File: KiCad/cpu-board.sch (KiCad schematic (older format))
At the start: 55 parts, among them CON1 BARREL_JACK, J1 Conn_FT245R, SW1 SW_PUSH_SMALL, SW2 SWITCH_INV, SW3 SW_PUSH_SMALL, U1 68008D, U10 GAL22V10, U11 74LS244, U12 LM555, U2 74LS08, U3 29F040B, U4 BS62LV4006, U5 74LS32, U6 74LS139, U7 74LS00, U8 74LS32, U9 74LS377, X1 OSCILLATOR

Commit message: add missing annotation
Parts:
- gave numbers to parts that had none: 2
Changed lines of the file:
@@
 	4400 1200 4400 1450
 $Comp
-L cpu-board-rescue:C C?
+L cpu-board-rescue:C C13
 U 1 1 5E6618CF
 P 4700 3750
-F 0 "C?" H 4700 3850 40  0000 L CNN
+F 0 "C13" H 4700 3850 40  0000 L CNN
 F 1 "0.1uF" H 4706 3665 40  0000 L CNN
 F 2 "Discret:C1" H 4738 3600 30  0001 C CNN
@@
 $EndComp
 $Comp
-L power:+5V #PWR?
+L power:+5V #PWR014
 U 1 1 5E662B43
 P 4700 3550
-F 0 "#PWR?" H 4700 3640 20  0001 C CNN
+F 0 "#PWR014" H 4700 3640 20  0001 C CNN
 F 1 "+5V" H 4700 3640 30  0000 C CNN
 F 2 "" H 4700 3550 60  0000 C CNN
@@
 $EndComp
 $Comp
-L cpu-board-rescue:GND #PWR?
+L cpu-board-rescue:GND #PWR019
 U 1 1 5E66313D
 P 4700 3950
-F 0 "#PWR?" H 4700 3950 30  0001 C CNN
+F 0 "#PWR019" H 4700 3950 30  0001 C CNN
 F 1 "GND" H 4700 3880 30  0001 C CNN
 F 2 "" H 4700 3950 60  0000 C CNN
@@
 $EndComp
 $Comp
-L cpu-board-rescue:C C?
+L cpu-board-rescue:C C14
 U 1 1 5E666AC0
 P 8500 4550
-F 0 "C?" H 8500 4650 40  0000 L CNN
+F 0 "C14" H 8500 4650 40  0000 L CNN
 F 1 "0.1uF" H 8506 4465 40  0000 L CNN
 F 2 "Discret:C1" H 8538 4400 30  0001 C CNN
@@
 $EndComp
 $Comp
-L power:+5V #PWR?
+L power:+5V #PWR021
 U 1 1 5E666AC6
 P 8500 4350
-F 0 "#PWR?" H 8500 4440 20  0001 C CNN
+F 0 "#PWR021" H 8500 4440 20  0001 C CNN
 F 1 "+5V" H 8500 4440 30  0000 C CNN
 F 2 "" H 8500 4350 60  0000 C CNN
@@
 $EndComp
 $Comp
-L cpu-board-rescue:GND #PWR?
+L cpu-board-rescue:GND #PWR025
 U 1 1 5E666ACC
 P 8500 4750
-F 0 "#PWR?" H 8500 4750 30  0001 C CNN
+F 0 "#PWR025" H 8500 4750 30  0001 C CNN
 F 1 "GND" H 8500 4680 30  0001 C CNN
 F 2 "" H 8500 4750 60  0000 C CNN

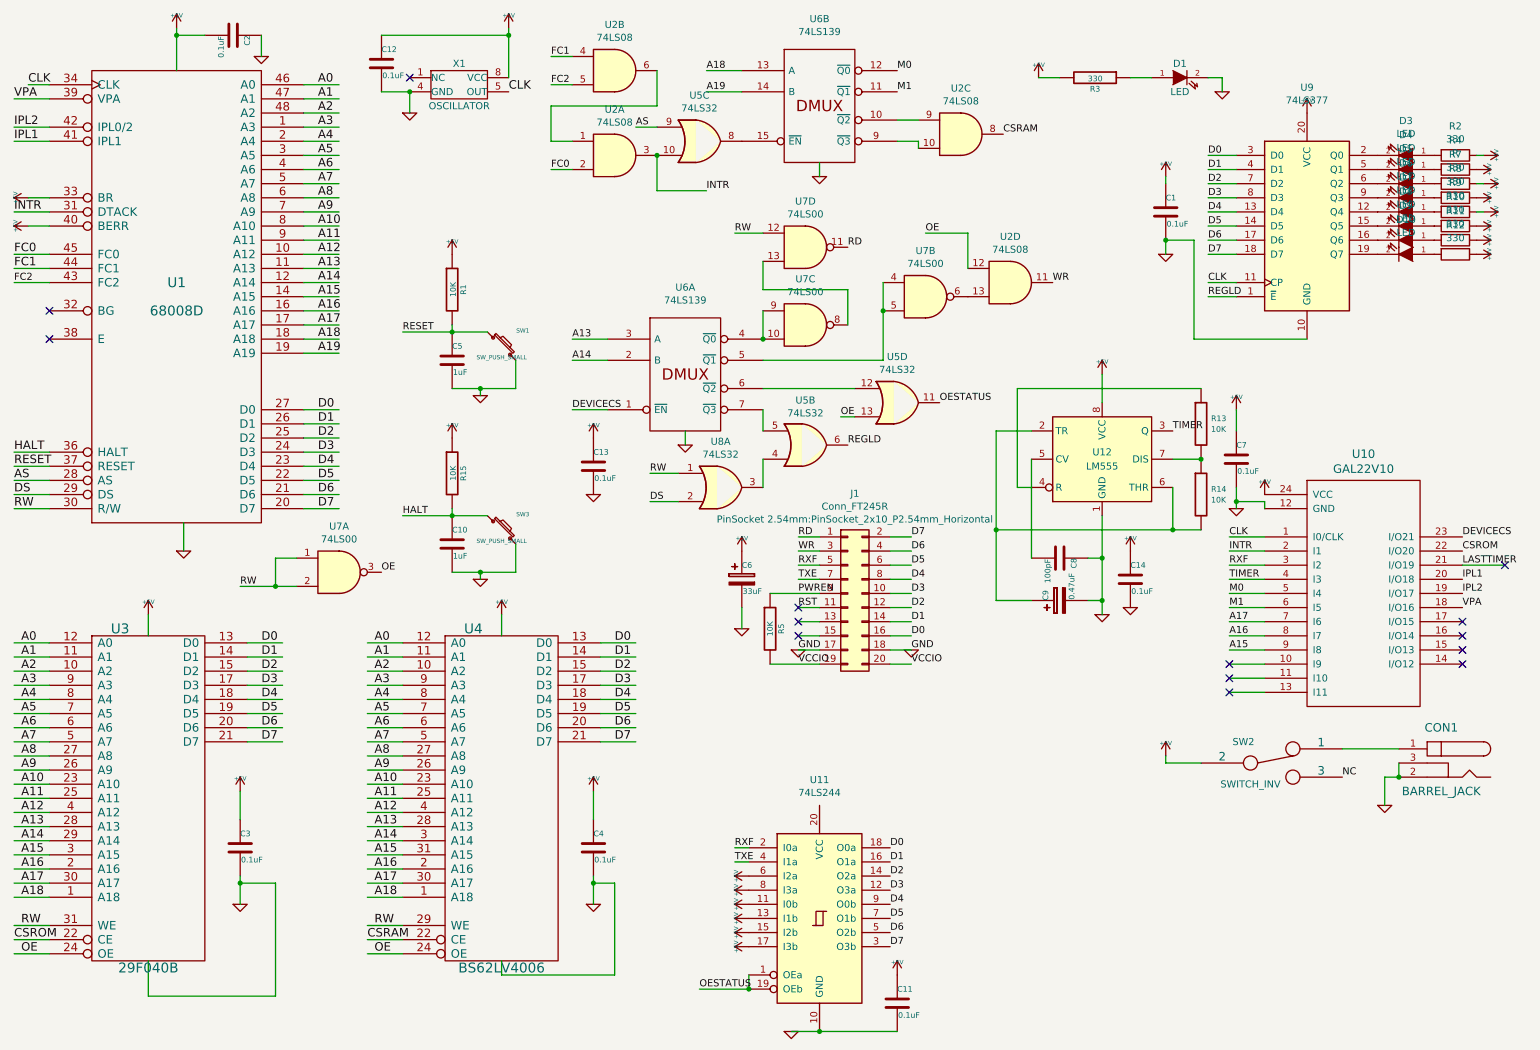
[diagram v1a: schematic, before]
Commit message: add footprints to schema, add chips to board layout
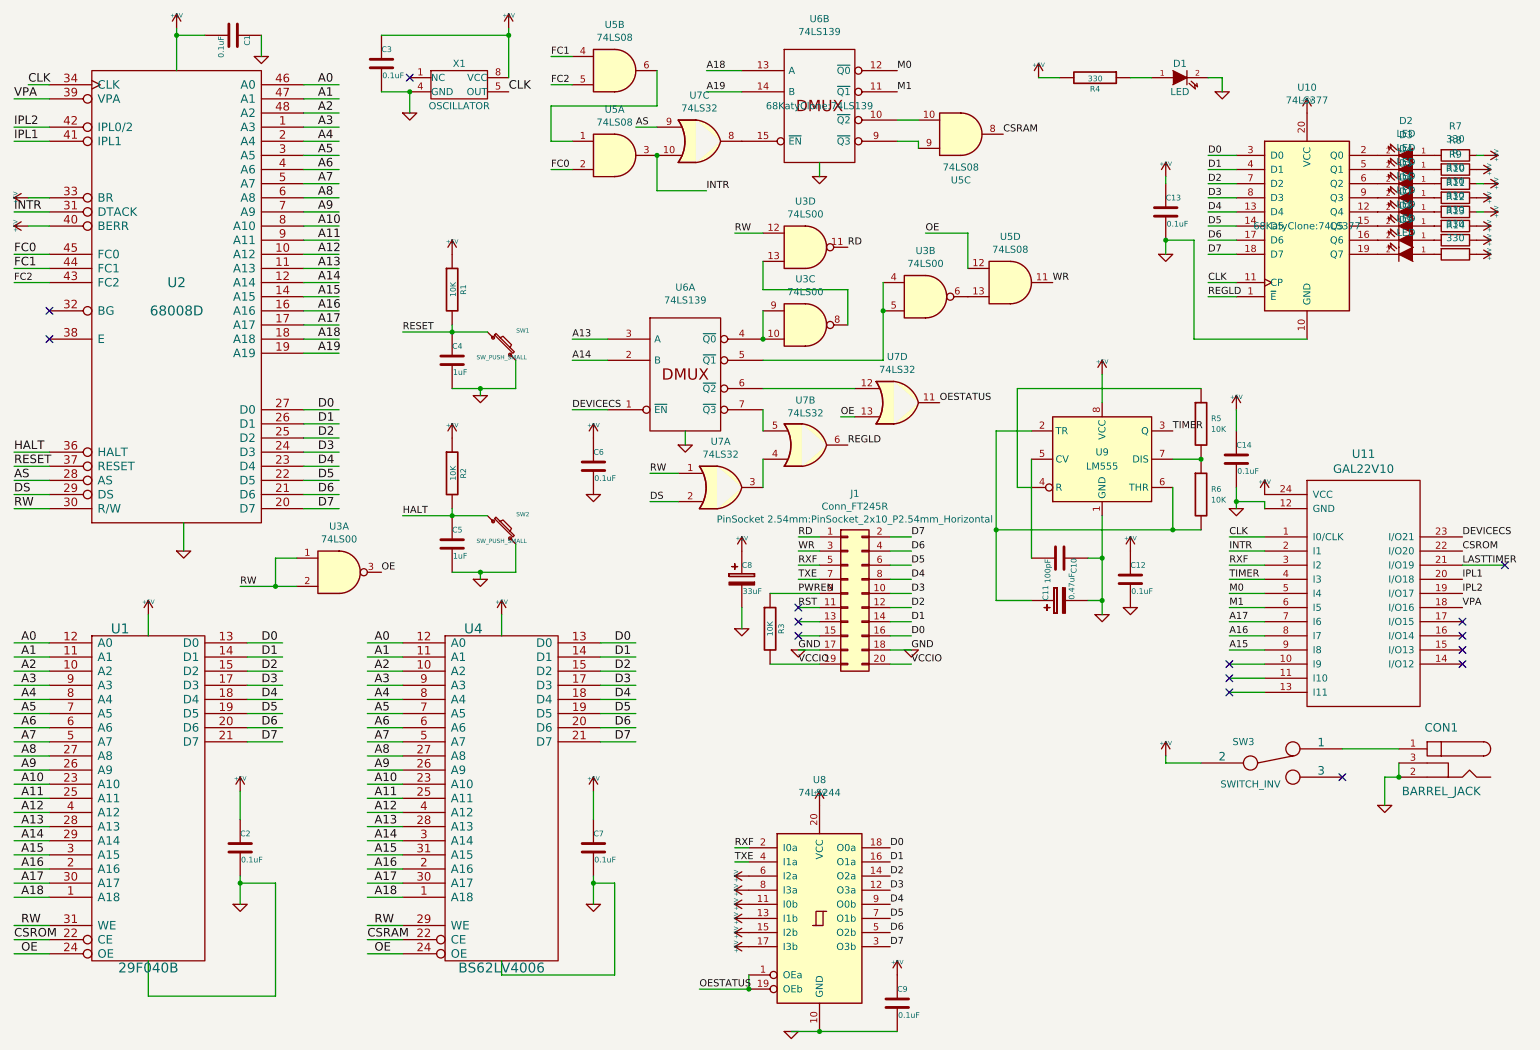
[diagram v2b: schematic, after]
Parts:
- U1: renamed from U3; footprint Sockets_DIP:DIP-32__600_ELL -> 68KatyClone:DIP-32_W15.24mm_Socket_LongPads
- U10: renamed from U9; footprint (none) -> 68KatyClone:74LS377
- U11: renamed from U10; footprint (none) -> 68KatyClone:GAL22V10
- U2: renamed from U1; footprint Sockets_DIP:DIP-48__600_ELL -> 68KatyClone:DIP-48_W15.24mm_Socket_LongPads
- U3: renamed from U7; footprint (none) -> 68KatyClone:DIP-14_W7.62mm_Socket_LongPads
- U4: footprint Sockets_DIP:DIP-32__600_ELL -> 68KatyClone:DIP-32_W15.24mm_Socket_LongPads
- U5: renamed from U2; footprint (none) -> 68KatyClone:DIP-14_W7.62mm_Socket_LongPads
- U6: footprint (none) -> 68KatyClone:74LS139
- U7: renamed from U5; footprint (none) -> 68KatyClone:DIP-14_W7.62mm_Socket_LongPads
- U7: renamed from U8; footprint (none) -> 68KatyClone:DIP-14_W7.62mm_Socket_LongPads
- U9: renamed from U12; footprint (none) -> 68KatyClone:DIP-8_W7.62mm_Socket_LongPads
- X1: footprint Sockets_DIP:DIP-8__300_ELL -> 68KatyClone:DIP-8_W7.62mm_Socket_LongPads
- renumbered C2 to C1, C8 to C10, C9 to C11, C14 to C12, C1 to C13, C7 to C14, C3 to C2, C12 to C3, C5 to C4, C10 to C5, C13 to C6, C4 to C7, C6 to C8, C11 to C9, D3 to D2, D4 to D3, D5 to D4, D6 to D5, D7 to D6, D8 to D7, D9 to D8, D10 to D9, R8 to R10, R9 to R11, R10 to R12, R11 to R13, R12 to R14, R15 to R2, R5 to R3, R3 to R4, R13 to R5, R14 to R6, R2 to R7, R4 to R8, R7 to R9, SW3 to SW2, SW2 to SW3, U11 to U8
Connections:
- net labels removed: NC
- no-connect marks 14 -> 15

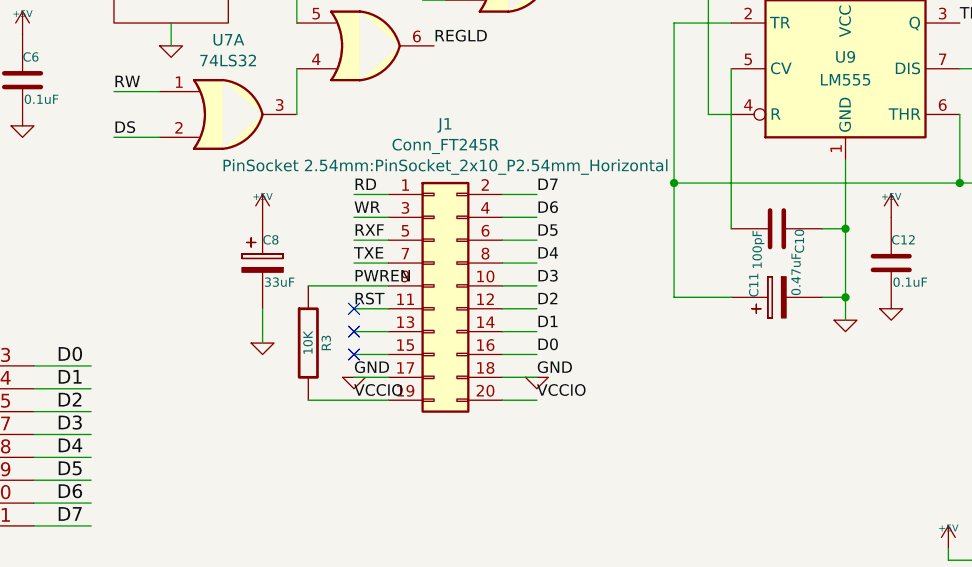
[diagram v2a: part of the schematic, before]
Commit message: add missing pull-up resistors for TXE and RXF
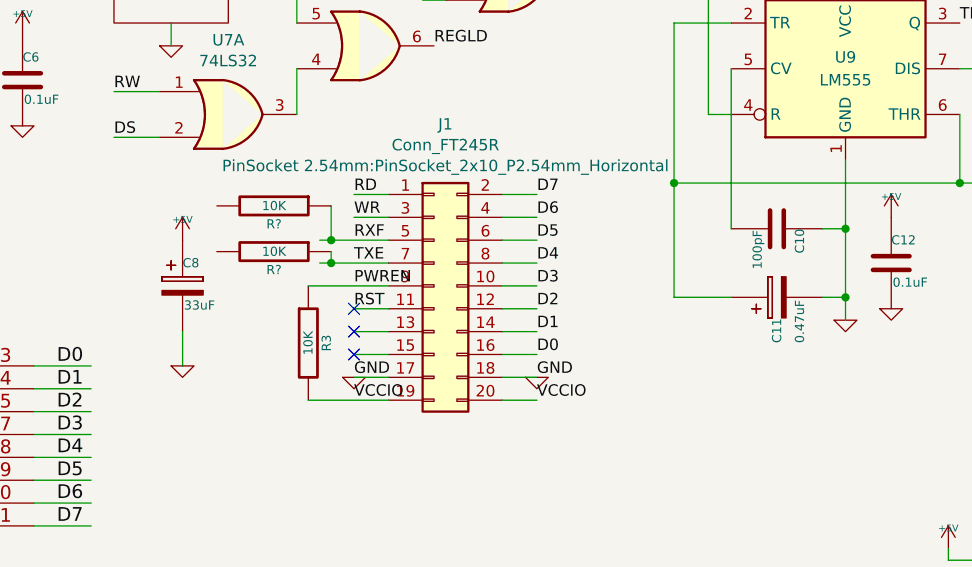
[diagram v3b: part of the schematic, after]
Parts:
- added R? (x2): 10K, Discret:R3-5, symbol cpu-board-rescue:R
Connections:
- wire segments 274 -> 278
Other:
- moved on the sheet: C8
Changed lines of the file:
@@
 L cpu-board-rescue:CP2 C8
 U 1 1 54869317
-P 5750 4550
-F 0 "C8" H 5750 4650 40  0000 L CNN
-F 1 "33uF" H 5756 4465 40  0000 L CNN
-F 2 "Discret:C1" H 5788 4400 30  0001 C CNN
-F 3 "" H 5750 4550 60  0000 C CNN
-	1    5750 4550
+P 5400 4650
+F 0 "C8" H 5400 4750 40  0000 L CNN
+F 1 "33uF" H 5406 4565 40  0000 L CNN
+F 2 "Discret:C1" H 5438 4500 30  0001 C CNN
+F 3 "" H 5400 4650 60  0000 C CNN
+	1    5400 4650
 	1    0    0    -1
 $EndComp
@@
 L power:+5V #PWR021
 U 1 1 548819AF
-P 5750 4350
-F 0 "#PWR021" H 5750 4440 20  0001 C CNN
-F 1 "+5V" H 5750 4440 30  0000 C CNN
-F 2 "" H 5750 4350 60  0000 C CNN
-F 3 "" H 5750 4350 60  0000 C CNN
-	1    5750 4350
+P 5400 4450
+F 0 "#PWR021" H 5400 4540 20  0001 C CNN
+F 1 "+5V" H 5400 4540 30  0000 C CNN
+F 2 "" H 5400 4450 60  0000 C CNN
+F 3 "" H 5400 4450 60  0000 C CNN
+	1    5400 4450
 	1    0    0    -1
 $EndComp
@@
 L cpu-board-rescue:GND #PWR022
 U 1 1 54885C31
-P 5750 4900
-F 0 "#PWR022" H 5750 4900 30  0001 C CNN
-F 1 "GND" H 5750 4830 30  0001 C CNN
-F 2 "" H 5750 4900 60  0000 C CNN
-F 3 "" H 5750 4900 60  0000 C CNN
-	1    5750 4900
+P 5400 5000
+F 0 "#PWR022" H 5400 5000 30  0001 C CNN
+F 1 "GND" H 5400 4930 30  0001 C CNN
+F 2 "" H 5400 5000 60  0000 C CNN
+F 3 "" H 5400 5000 60  0000 C CNN
+	1    5400 5000
 	1    0    0    -1
 $EndComp
@@
 	4700 6050 4700 6250
 Wire Wire Line
-	5750 4750 5750 4900
+	5400 4850 5400 5000
 Wire Wire Line
 	9250 3900 9250 4000
@@
 U 1 1 5DF4F7B4
 P 8000 4700
-F 0 "C11" H 8000 4800 40  0000 L CNN
-F 1 "0.47uF" H 8006 4615 40  0000 L CNN
+F 0 "C11" H 7800 4700 40  0000 L CNN
+F 1 "0.47uF" H 7800 4600 40  0000 L CNN
 F 2 "Discret:C1" H 8038 4550 30  0001 C CNN
 F 3 "" H 8000 4700 60  0000 C CNN
@@
 	6300 4350 6150 4350
 Wire Wire Line
-	6300 4450 6150 4450
-Wire Wire Line
-	6300 4550 6150 4550
-Wire Wire Line
 	6300 4750 6150 4750
 Wire Wire Line
@@
 	1    0    0    1
 $EndComp
+Wire Wire Line
+	6000 4450 6050 4450
+Wire Wire Line
+	6000 4550 6050 4550
+$Comp
+L cpu-board-rescue:R R?
+U 1 1 5E78BFBC
+P 5800 4300
+F 0 "R?" V 5880 4300 40  0000 C CNN
+F 1 "10K" V 5800 4300 40  0000 C CNN
+F 2 "Discret:R3-5" V 5730 4300 30  0001 C CNN
+F 3 "" H 5800 4300 30  0000 C CNN
+	1    5800 4300
+	0    1    1    0
+$EndComp
+$Comp
+L cpu-board-rescue:R R?
+U 1 1 5E7D729D
+P 5800 4500
+F 0 "R?" V 5880 4500 40  0000 C CNN
+F 1 "10K" V 5800 4500 40  0000 C CNN
+F 2 "Discret:R3-5" V 5730 4500 30  0001 C CNN
+F 3 "" H 5800 4500 30  0000 C CNN
+	1    5800 4500
+	0    1    1    0
+$EndComp
+Wire Wire Line
+	6050 4300 6050 4450
+Connection ~ 6050 4450
+Wire Wire Line
+	6050 4450 6300 4450
+Wire Wire Line
+	6050 4500 6050 4550
+Connection ~ 6050 4550
+Wire Wire Line
+	6050 4550 6300 4550
 $EndSCHEMATC
